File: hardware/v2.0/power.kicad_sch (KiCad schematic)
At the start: 58 parts, among them U1 ECP5U-25F-CABGA256, U2 LTC3407AEDD-2_PBF, U3 TLV62569DBV, U5 TCR5FM18A

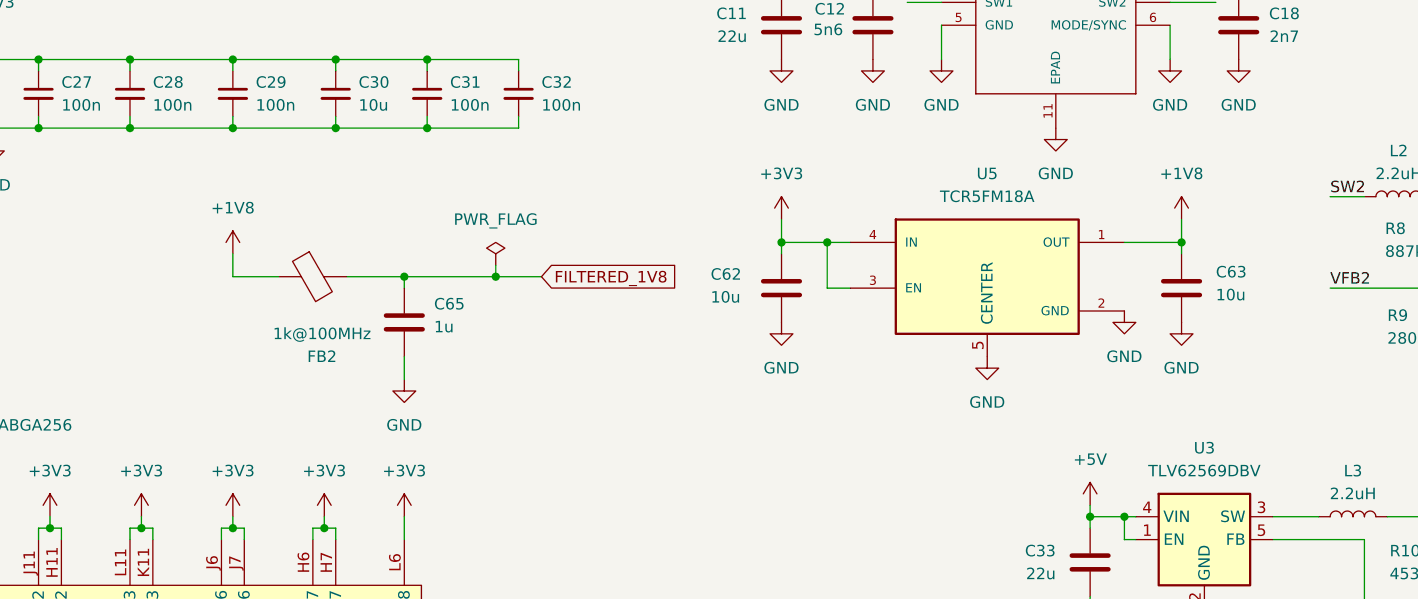
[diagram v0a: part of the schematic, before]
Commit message: ADC digital line power fix
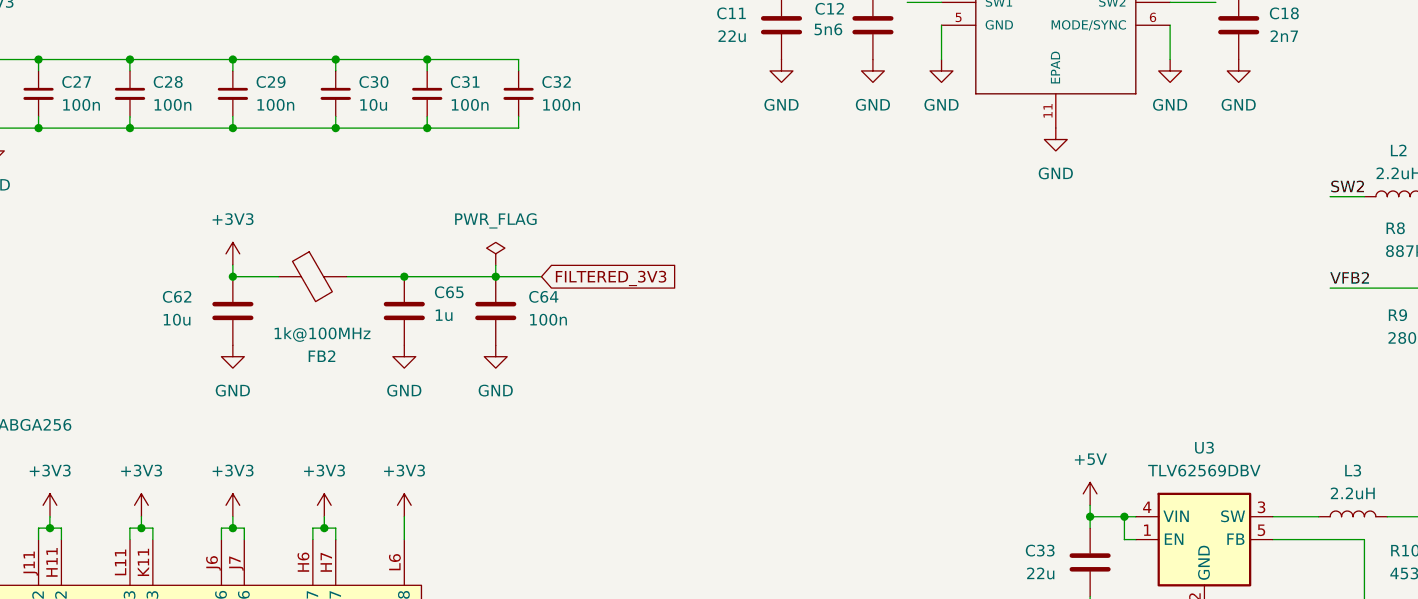
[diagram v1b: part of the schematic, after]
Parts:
- removed C63: 10u, Capacitor_SMD:C_0603_1608Metric, symbol Device:C
- removed U5: TCR5FM18A, TCR5FM50A:TCR5FM50A, symbol TCR5FM18A:TCR5FM18A
- added C64: 100n, Capacitor_SMD:C_0402_1005Metric, symbol Device:C
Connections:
- net +1V8 is gone; now on net +3V3: FB2.1
- net GND: now also C64.1
- net FILTERED_1V8 renamed FILTERED_3V3
- net FILTERED_3V3: now also C64.2
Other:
- moved on the sheet: C62, C65

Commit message: JLCPCB profile
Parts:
- R55: LCSC Part # C25744 -> C25741
- U1: LCSC Part # (none) -> C1521614
- U2: LCSC Part # (none) -> C684618
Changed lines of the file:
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@@
 	(title_block
 		(title "GammaPi Zero")
-		(date "2026-02-08")
-		(rev "v2.7.0")
+		(date "2026-02-28")
+		(rev "v2.7.1")
 		(company "Vadym Vikulin, Chengyin Yao (cheyao)")
 		(comment 1 "https://github.com/vikulin/gammapi-zero")
@@
 			)
 		)
+		(property "LCSC Part #" "C684618"
+			(at 181.61 69.85 0)
+			(effects
+				(font
+					(size 1.27 1.27)
+				)
+				(hide yes)
+			)
+		)
 		(pin "2"
 		)
@@
 			)
 		)
+		(property "LCSC Part #" "C1521614"
+			(at 80.01 152.4 0)
+			(effects
+				(font
+					(size 1.27 1.27)
+				)
+				(hide yes)
+			)
+		)
 		(pin "T2"
 		)
@@
 			)
 		)
-		(property "LCSC Part #" "C25744"
+		(property "LCSC Part #" "C25741"
 			(at 223.52 60.96 0)
 			(effects

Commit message: ADA4932-1 amplifier
ADA4932-1 amplifier replaced LTC6409
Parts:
- C12: LCSC Part # C307435 -> C3878619; MANUFACTURER Samsung Electro-Mechanics -> muRata; MANUFACTURER_PART_NUMBER CL05B562KB5NNNC -> GRM1555C1H562GE01D
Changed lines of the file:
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@@
 			)
 		)
-		(property "LCSC Part #" "C307435"
+		(property "LCSC Part #" "C3878619"
 			(at 177.8 80.01 0)
 			(effects
@@
 			)
 		)
-		(property "MANUFACTURER" "Samsung Electro-Mechanics"
+		(property "MANUFACTURER" "muRata"
 			(at 177.8 80.01 0)
 			(effects
@@
 			)
 		)
-		(property "MANUFACTURER_PART_NUMBER" "CL05B562KB5NNNC"
+		(property "MANUFACTURER_PART_NUMBER" "GRM1555C1H562GE01D"
 			(at 177.8 80.01 0)
 			(effects

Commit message: TLV62569DBVR Voltage Regulator
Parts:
- removed R53, R54: 4M7, Resistor_SMD:R_0402_1005Metric, symbol Device:R
- removed R55: 100k, Resistor_SMD:R_0402_1005Metric, symbol Device:R
- removed U2: LTC3407AEDD-2_PBF, LTC3407AEDD-2_PBF:DFN-10_DD, symbol LTC3407AEDD-2_PBF:LTC3407AEDD-2_PBF
- added U2, U3: TLV62569DBV, Package_TO_SOT_SMD:SOT-23-5, symbol Regulator_Switching:TLV62569DBV
- C12: value 5n6 -> 22u; footprint Capacitor_SMD:C_0402_1005Metric -> Capacitor_SMD:C_0603_1608Metric; LCSC Link https://www.lcsc.com/product-detail/C307435.html -> https://lcsc.com/product-detail/Multilayer-Ceramic-Capacito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; LCSC Part # C3878619 -> C59461; MANUFACTURER muRata -> Samsung Electro-Mechanics; MANUFACTURER_PART_NUMBER GRM1555C1H562GE01D -> CL10A226MQ8NRNC; Manufactuer Part Number CL05B562KB5NNNC -> CL10A226MQ8NRNC
- C18: value 2n7 -> 22u; footprint Capacitor_SMD:C_0402_1005Metric -> Capacitor_SMD:C_0603_1608Metric; LCSC Link https://www.lcsc.com/product-detail/C84704.html -> https://lcsc.com/product-detail/Multilayer-Ceramic-Capacito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; LCSC Part # C84704 -> C59461; MANUFACTURER_PART_NUMBER CL05B272KB5NNNC -> CL10A226MQ8NRNC; Manufactuer Part Number CL05B272KB5NNNC -> CL10A226MQ8NRNC
- C56, C57: value 22p -> 100p; LCSC Link https://www.lcsc.com/product-detail/C70464.html -> https://www.lcsc.com/product-detail/C26409.html; LCSC Part # C70464 -> C26409; MANUFACTURER_PART_NUMBER CL05C220JB5NNNC -> CL05C101JB5NNNC; Manufactuer Part Number CL05C220JB5NNNC -> CL05C101JB5NNNC
- C58: value 6.8p -> 100p; LCSC Link https://www.lcsc.com/product-detail/C318598.html -> https://www.lcsc.com/product-detail/C26409.html; LCSC Part # C318598 -> C26409; MANUFACTURER_PART_NUMBER CL05C6R8CB5NNNC -> CL05C101JB5NNNC; Manufactuer Part Number CL05C6R8CB5NNNC -> CL05C101JB5NNNC
- R10: value 453k -> 15k; LCSC Link https://www.lcsc.com/product-detail/C27009.html -> https://lcsc.com/product-detail/Chip-Resistor-Surface-Mount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; LCSC Part # C27009 -> C25756; MANUFACTURER_PART_NUMBER 0402WGF4533TCE -> 0402WGF1502TCE; Manufactuer Part Number 0402WGF4533TCE -> 0402WGF1502TCE
- R11: value 100k -> 3.3k; LCSC Link https://www.lcsc.com/product-detail/C25741.html -> https://lcsc.com/product-detail/Chip-Resistor-Surface-Mount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; LCSC Part # C25741 -> C25890; MANUFACTURER_PART_NUMBER 0402WGF1003TCE -> 0402WGF3301TCE; Manufactuer Part Number 0402WGF1003TCE -> 0402WGF3301TCE
- R6: value 255k -> 15k; LCSC Link https://www.lcsc.com/product-detail/C270623.html -> https://lcsc.com/product-detail/Chip-Resistor-Surface-Mount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; LCSC Part # C270623 -> C25756; MANUFACTURER_PART_NUMBER 0402WGF2553TCE -> 0402WGF1502TCE; Manufactuer Part Number 0402WGF2553TCE -> 0402WGF1502TCE
- R7: value 301k -> 18k; LCSC Link https://www.lcsc.com/product-detail/C25775.html -> https://www.lcsc.com/product-detail/C25762.html; LCSC Part # C25775 -> C25762; MANUFACTURER_PART_NUMBER 0402WGF3013TCE -> 0402WGF1802TCE; Manufactuer Part Number 0402WGF3013TCE -> 0402WGF1802TCE
- R8: value 887k -> 15k; LCSC Link https://www.lcsc.com/product-detail/C423127.html -> https://lcsc.com/product-detail/Chip-Resistor-Surface-Mount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; LCSC Part # C423127 -> C25756; MANUFACTURER_PART_NUMBER 0402WGF8873TCE -> 0402WGF1502TCE; Manufactuer Part Number 0402WGF8873TCE -> 0402WGF1502TCE
- R9: value 280k -> 4.7k; LCSC Link https://www.lcsc.com/product-detail/C46006.html -> https://lcsc.com/product-detail/Chip-Resistor-Surface-Mount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; LCSC Part # C46006 -> C25900; MANUFACTURER_PART_NUMBER 0402WGF2803TCE -> 0402WGF4701TCE; Manufactuer Part Number 0402WGF2803TCE -> 0402WGF4701TCE
- renumbered U3 to U4
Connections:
- net +1V1: now also C12.1
- net +5V: now also C18.1, U2.1 (EN), U2.4 (VIN), U3.1 (EN), U3.4 (VIN)
- net GND: now also C12.2, U2.2 (GND), U3.2 (GND); no longer C12.1
- net SW1: no longer names the net of L1.1
- net SW1: now also U2.3 (SW)
- net SW2: no longer names the net of L2.1
- net SW2: now also U3.3 (SW)
- net VFB1: no longer names the net of C56.2, R6.2, R7.1
- net VFB1: now also U2.5 (FB)
- net VFB2: no longer names the net of C57.2, R8.2, R9.1
- net VFB2: now also U3.5 (FB)
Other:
- note added: "(15/3.3+1)*0.6=3.3V"
- note added: "(15/4.7+1)*0.6=2.5V"
- note added: "(15k/18k+1)*0.6V = 1.1V"
- note removed: "(255/301+1)*0.6=1.1V"
- note removed: "(453/100+1)*0.6=3.3V"
- note removed: "(887/280+1)*0.6=2.5V"
- moved on the sheet: C11, C13, C14, C19, C20, C33, C34, C35, C56, C57, C58, L1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

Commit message: Capacitor update
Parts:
- C62: footprint Capacitor_SMD:C_0603_1608Metric -> Capacitor_SMD:C_0402_1005Metric; LCSC Link https://lcsc.com/product-detail/Multilayer-Ceramic-Capacito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 -> https://www.lcsc.com/product-detail/C315248.html; LCSC Part # C19702 -> C315248; MANUFACTURER_PART_NUMBER CL10A106KP8NNNC -> CL05A106MP5NUNC; Manufactuer Part Number CL10A106KP8NNNC -> CL05A106MP5NUNC
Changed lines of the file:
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@@
 			)
 		)
-		(property "Footprint" "Capacitor_SMD:C_0603_1608Metric"
+		(property "Footprint" "Capacitor_SMD:C_0402_1005Metric"
 			(at 105.7148 115.57 0)
 			(effects
@@
 			)
 		)
-		(property "Description" "10uF ±10% 10V Ceramic Capacitor X5R 0603"
+		(property "Description" "10uF ±20% 10V Ceramic Capacitor X5R 0402"
 			(at 106.68 111.76 0)
 			(effects
@@
 			)
 		)
-		(property "LCSC Part #" "C19702"
+		(property "LCSC Part #" "C315248"
 			(at 106.68 111.76 0)
 			(effects
@@
 			)
 		)
-		(property "LCSC Link" "https://lcsc.com/product-detail/Multilayer-Ceramic-Capacitors-MLCC-SMD-SMT_Samsung-Electro-Mechanics-CL10A106KP8NNNC_C19702.html"
+		(property "LCSC Link" "https://www.lcsc.com/product-detail/C315248.html"
 			(at 106.68 111.76 0)
 			(effects
@@
 			)
 		)
-		(property "Manufactuer Part Number" "CL10A106KP8NNNC"
+		(property "Manufactuer Part Number" "CL05A106MP5NUNC"
 			(at 106.68 111.76 0)
 			(effects
@@
 			)
 		)
-		(property "MANUFACTURER_PART_NUMBER" "CL10A106KP8NNNC"
+		(property "MANUFACTURER_PART_NUMBER" "CL05A106MP5NUNC"
 			(at 106.68 111.76 0)
 			(effects

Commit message: Pad adjustments
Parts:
- C2: footprint Capacitor_SMD:C_0603_1608Metric -> Capacitor_SMD:C_0402_1005Metric; LCSC Link https://lcsc.com/product-detail/Multilayer-Ceramic-Capacito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 -> https://www.lcsc.com/product-detail/C315248.html; LCSC Part # C19702 -> C315248; MANUFACTURER_PART_NUMBER CL10A106KP8NNNC -> CL05A106MP5NUNC; Manufactuer Part Number CL10A106KP8NNNC -> CL05A106MP5NUNC
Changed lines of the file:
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@@
-	)
-	(symbol
-		(lib_id "Device:C_Small")
-		(at 34.29 50.8 0)
-		(unit 1)
-		(exclude_from_sim no)
-		(in_bom yes)
-		(on_board yes)
-		(dnp no)
-		(property "Reference" "C2"
-			(at 35.052 49.022 0)
-			(effects
-				(font
-					(size 1.27 1.27)
-				)
-				(justify left)
-			)
-		)
-		(property "Value" "10u"
-			(at 35.052 52.832 0)
-			(effects
-				(font
-					(size 1.27 1.27)
-				)
-				(justify left)
-			)
-		)
-		(property "Footprint" "Capacitor_SMD:C_0603_1608Metric"
-			(at 34.29 50.8 0)
-			(effects
-				(font
-					(size 1.27 1.27)
-				)
-				(hide yes)
-			)
-		)
-		(property "Datasheet" "~"
-			(at 34.29 50.8 0)
-			(effects
-				(font
-					(size 1.27 1.27)
-				)
-				(hide yes)
-			)
-		)
-		(property "Description" "10uF ±10% 10V Ceramic Capacitor X5R 0603"
-			(at 34.29 50.8 0)
-			(effects
-				(font
-					(size 1.27 1.27)
-				)
-				(hide yes)
-			)
-		)
-		(property "LCSC Part #" "C19702"
-			(at 34.29 50.8 0)
-			(effects
-				(font
-					(size 1.27 1.27)
-				)
-				(hide yes)
-			)
-		)
-		(property "LCSC Link" "https://lcsc.com/product-detail/Multilayer-Ceramic-Capacitors-MLCC-SMD-SMT_Samsung-Electro-Mechanics-CL10A106KP8NNNC_C19702.html"
-			(at 34.29 50.8 0)
-			(effects
-				(font
-					(size 1.27 1.27)
-				)
-				(hide yes)
-			)
-		)
-		(property "Manufactuer Part Number" "CL10A106KP8NNNC"
-			(at 34.29 50.8 0)
-			(effects
-				(font
-					(size 1.27 1.27)
-				)
-				(hide yes)
-			)
-		)
-		(property "Note" ""
-			(at 34.29 50.8 0)
-			(effects
-				(font
-					(size 1.27 1.27)
-				)
-				(hide yes)
-			)
-		)
-		(property "Notes" ""
-			(at 34.29 50.8 0)
-			(effects
-				(font
-					(size 1.27 1.27)
-				)
-				(hide yes)
-			)
-		)
-		(property "Original" ""
-			(at 34.29 50.8 0)
-			(effects
-				(font
-					(size 1.27 1.27)
-				)
-				(hide yes)
-			)
-		)
-		(property "Instructions/Notes" ""
-			(at 34.29 50.8 0)
-			(effects
-				(font
-					(size 1.27 1.27)
-				)
-				(hide yes)
-			)
-		)
-		(property "MANUFACTURER_PART_NUMBER" "CL10A106KP8NNNC"
-			(at 34.29 50.8 0)
-			(effects
-				(font
-					(size 1.27 1.27)
-				)
-				(hide yes)
-			)
-		)
-		(property "MANUFACTURER" "Samsung Electro-Mechanics"
-			(at 34.29 50.8 0)
-			(effects
-				(font
-					(size 1.27 1.27)
-				)
-				(hide yes)
-			)
-		)
-		(property "VENDOR" ""
-			(at 34.29 50.8 0)
-			(effects
-				(font
-					(size 1.27 1.27)
-				)
-				(hide yes)
-			)
-		)
-		(pin "1"
-		)
-		(pin "2"
-		)
-		(instances
-			(project "gammapi-zero"
-				(path "/f88da08e-cf42-4d03-a08f-3f602fe6658d/a9c02a11-f344-487c-ac67-1be6ae5dcf49"
-					(reference "C2")
-					(unit 1)
-				)
-			)
-		)
 	)
 	(symbol
@@
 					(unit 1)
 				)
+			)
+		)
+	)
+	(symbol
+		(lib_id "Device:C_Small")
+		(at 34.29 50.8 0)
+		(mirror y)
+		(unit 1)
+		(exclude_from_sim no)
+		(in_bom yes)
+		(on_board yes)
+		(dnp no)
+		(property "Reference" "C2"
+			(at 26.416 49.276 0)
+			(effects
+				(font
+					(size 1.27 1.27)
+				)
+				(justify right)
+			)
+		)
+		(property "Value" "10u"
+			(at 26.416 51.816 0)
+			(effects
+				(font
+					(size 1.27 1.27)
+				)
+				(justify right)
+			)
+		)
+		(property "Footprint" "Capacitor_SMD:C_0402_1005Metric"
+			(at 34.29 50.8 0)
+			(effects
+				(font
+					(size 1.27 1.27)
+				)
+				(hide yes)
+			)
+		)
+		(property "Datasheet" "~"
+			(at 34.29 50.8 0)
+			(effects
+				(font
+					(size 1.27 1.27)
+				)
+				(hide yes)
+			)
+		)
+		(property "Description" "Unpolarized capacitor, small symbol"
+			(at 34.29 50.8 0)
+			(effects
+				(font
+					(size 1.27 1.27)
+				)
+				(hide yes)
+			)
+		)
+		(property "LCSC Part #" "C315248"
+			(at 34.29 50.8 0)
+			(effects
+				(font
+					(size 1.27 1.27)
+				)
+				(hide yes)
+			)
+		)
+		(property "LCSC Link" "https://www.lcsc.com/product-detail/C315248.html"
+			(at 34.29 50.8 0)
+			(effects
+				(font
+					(size 1.27 1.27)
+				)
+				(hide yes)
+			)
+		)
+		(property "Manufactuer Part Number" "CL05A106MP5NUNC"
+			(at 34.29 50.8 0)
+			(effects
+				(font
+					(size 1.27 1.27)
+				)
+				(hide yes)
+			)
+		)
+		(property "Note" ""
+			(at 34.29 50.8 0)
+			(effects
+				(font
+					(size 1.27 1.27)
+				)
+				(hide yes)
+			)
+		)
+		(property "Notes" ""
+			(at 34.29 50.8 0)
+			(effects
+				(font
+					(size 1.27 1.27)
+				)
+				(hide yes)
+			)
+		)
+		(property "Original" ""
+			(at 34.29 50.8 0)
+			(effects
+				(font
+					(size 1.27 1.27)
+				)
+				(hide yes)
+			)
+		)
+		(property "Instructions/Notes" ""
+			(at 34.29 50.8 0)
+			(effects
+				(font
+					(size 1.27 1.27)
+				)
+				(hide yes)
+			)
+		)
+		(property "MANUFACTURER_PART_NUMBER" "CL05A106MP5NUNC"
+			(at 34.29 50.8 0)
+			(effects
+				(font
+					(size 1.27 1.27)
+				)
+				(hide yes)
+			)
+		)
+		(property "MANUFACTURER" "Samsung Electro-Mechanics"
+			(at 34.29 50.8 0)
+			(effects
+				(font
+					(size 1.27 1.27)
+				)
+				(hide yes)
+			)
+		)
+		(property "VENDOR" ""
+			(at 34.29 50.8 0)
+			(effects
+				(font
+					(size 1.27 1.27)
+				)
+				(hide yes)
+			)
+		)
+		(pin "2"
+		)
+		(pin "1"
+		)
+		(instances
+			(project "gammapi-zero"
+				(path "/f88da08e-cf42-4d03-a08f-3f602fe6658d/a9c02a11-f344-487c-ac67-1be6ae5dcf49"
+					(reference "C2")
+					(unit 1)
+				)
